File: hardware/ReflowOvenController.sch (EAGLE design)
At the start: 27 parts, among them U1 VSK-S5, U2 MAX31856, U3 LTV-354T, U4 FODM3053, U5 T25

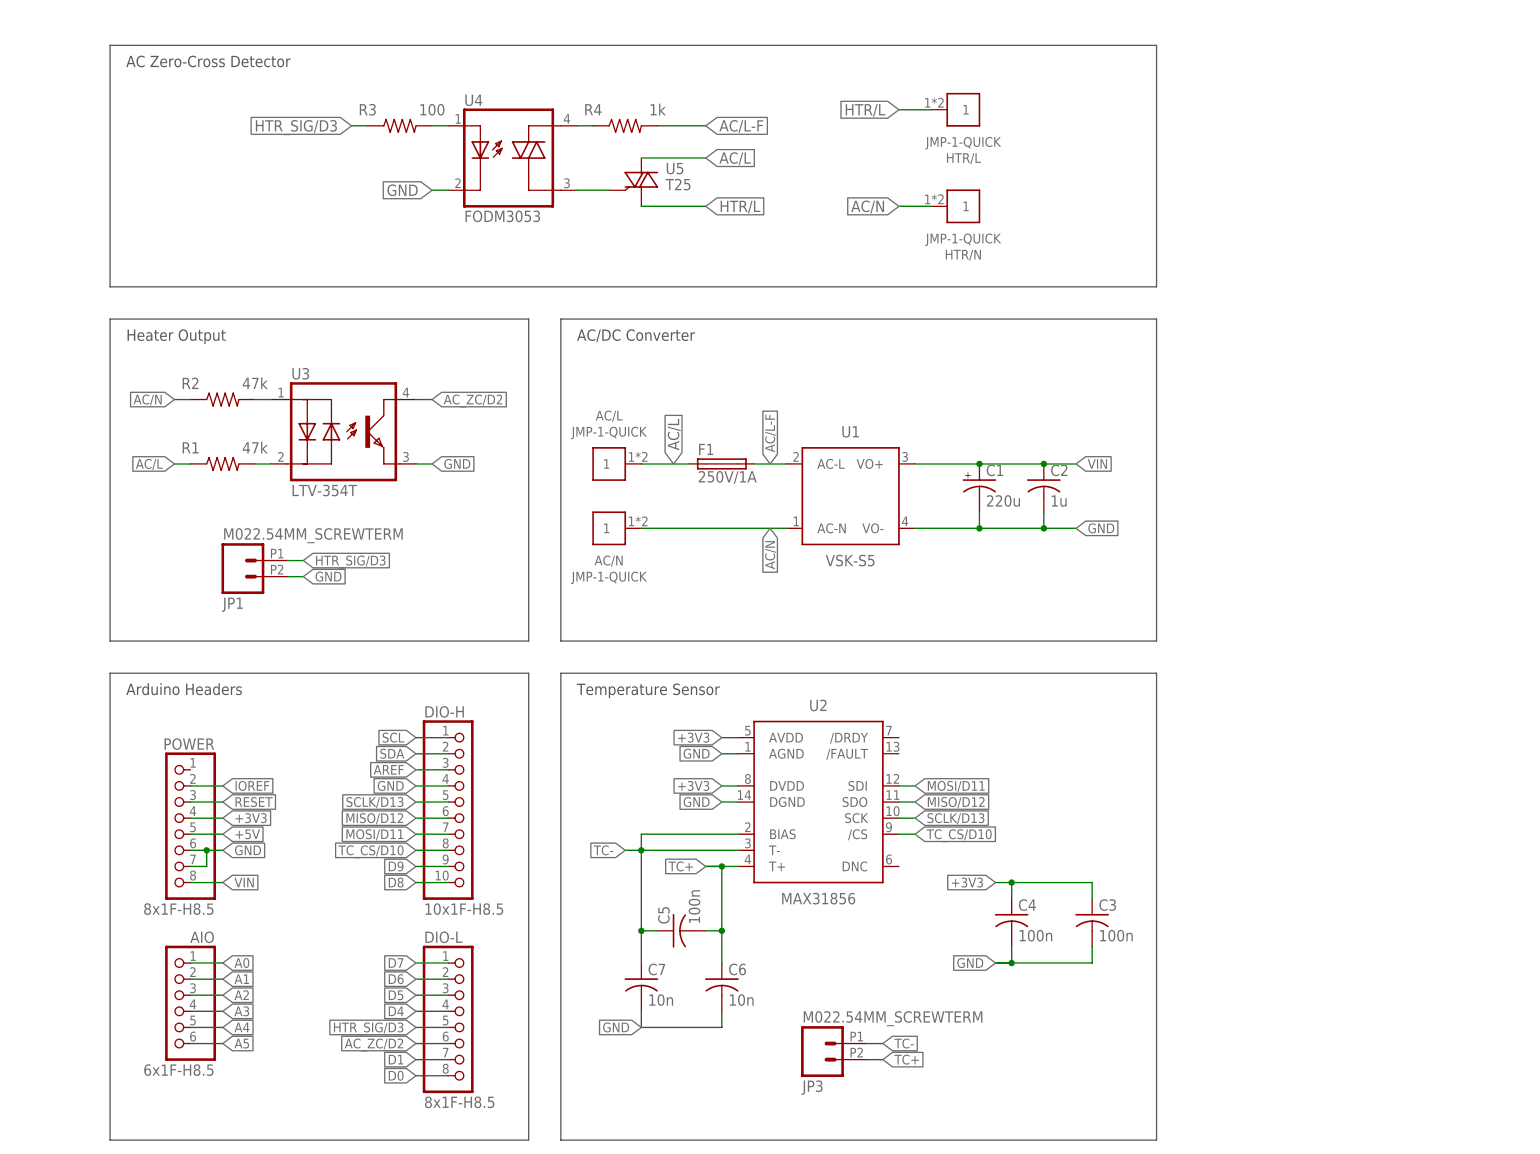
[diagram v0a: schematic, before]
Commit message: Improved mechanical layout. Added status leds.
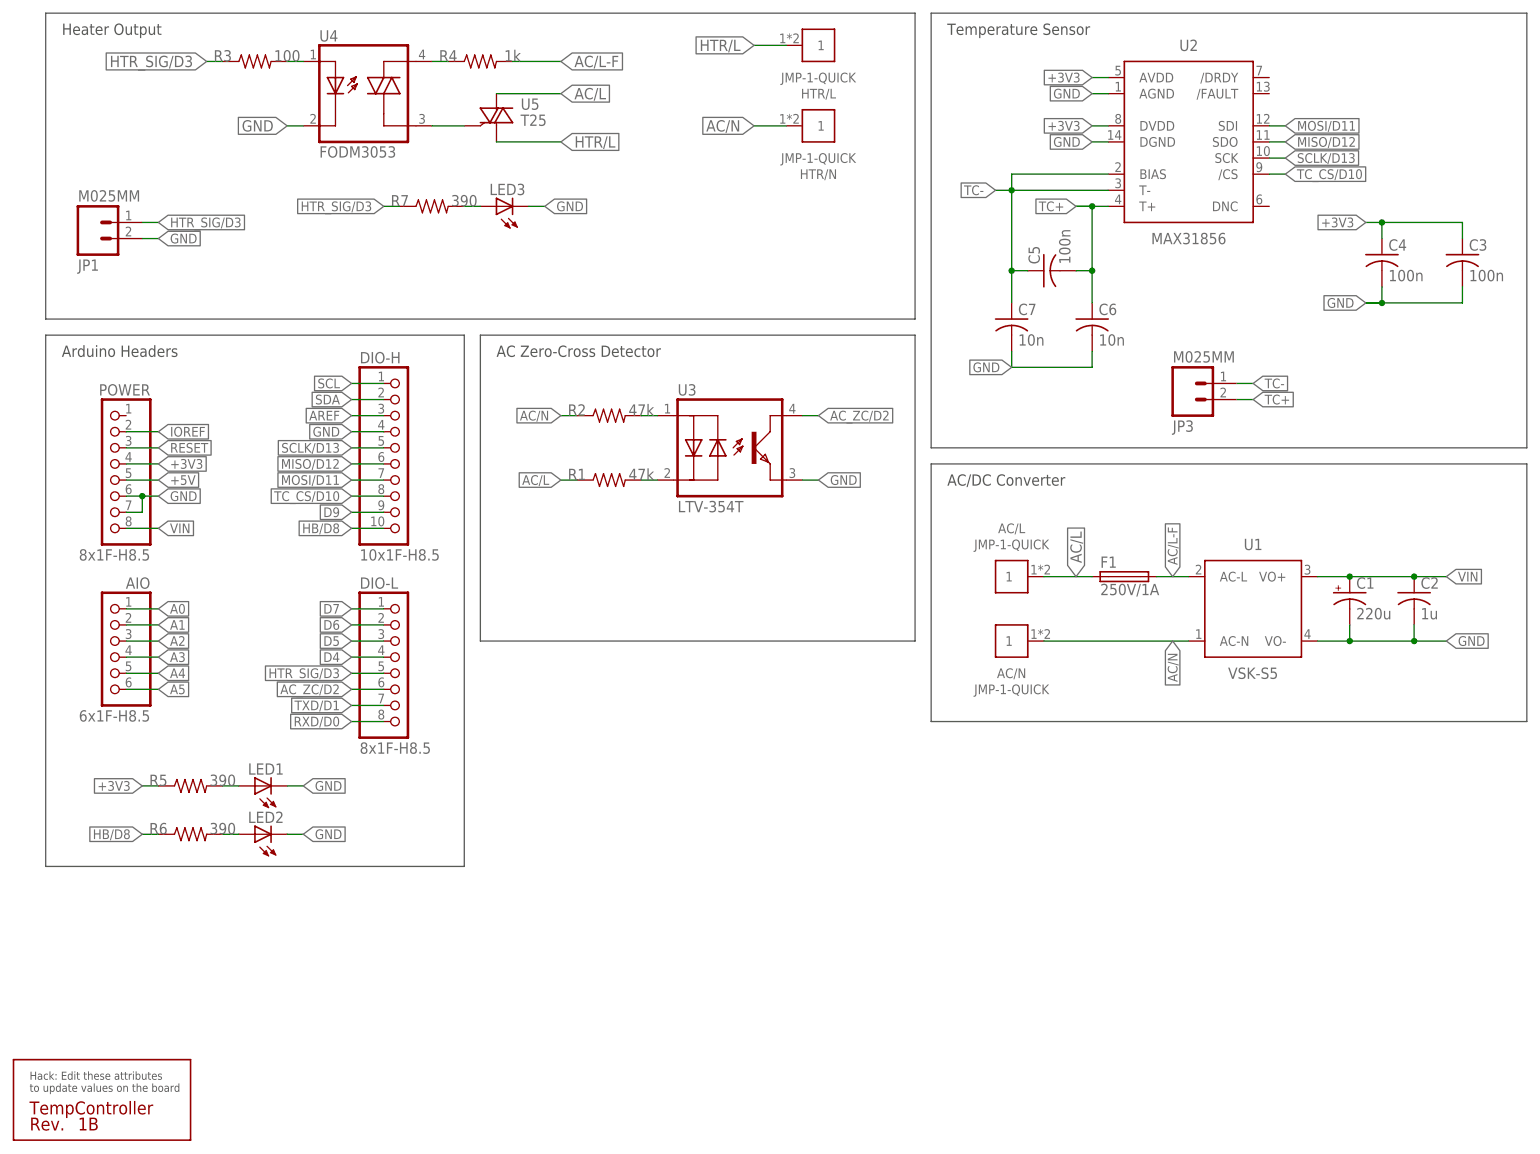
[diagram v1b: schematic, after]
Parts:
- added LED1, LED2, LED3: (no value), SmslsTron:LEDCHIP-LED0805
- added R5, R6, R7: 390, SmslsTron:R-US_R0805
- added U$1: SILK_QC, SmslsTron:SILK_QC
- JP1, JP3: value M022.54MM_SCREWTERM -> M025MM; device ReflowOvenController:M022.54MM_SCREWTERM -> SmslsTron:M025MM
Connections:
- net D0 renamed RXD/D0
- net D1 renamed TXD/D1
- removed net D8: DIO-H.10
- new net HB/D8: DIO-H.10, R6.1
- new net N$6: LED3.A, R7.2
- new net N$7: LED1.A, R5.2
- new net N$9: LED2.A, R6.2
- net +3V3: now also R5.1
- net GND: now also LED1.C, LED2.C, LED3.C
- net HTR_SIG/D3: now also R7.1
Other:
- moved on the sheet: AC/L, AC/N, AIO, C1, C2, C3, C4, C5, C6, C7, DIO-H, DIO-L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
